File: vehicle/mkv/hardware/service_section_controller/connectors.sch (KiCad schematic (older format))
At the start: 5 parts, among them J401 MM_F_VT_16, J402 MM_F_VT_18, J403 MicroFit_VT_12, J404 Ultrafit_4_RA, J405 Ultrafit_4_RA

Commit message: incorporated feedback from dr
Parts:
- removed J402: MM_F_VT_18, footprints:micromatch_female_vert_18, symbol formula:MM_F_VT_18
- added J402: MM_F_VT_14, footprints:micromatch_female_vert_14, symbol formula:MM_F_VT_14
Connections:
- wire segments 13 -> 22
- no-connect marks 3 -> 0
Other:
- note added: "This needs to be a right angle connector"
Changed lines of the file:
@@
 Text GLabel 9050 1800 2    50   Input ~ 0
 FINAL_SHUTDOWN
-Text GLabel 6750 2750 2    50   Input ~ 0
+Text GLabel 6850 2050 2    50   Input ~ 0
 CHARGE_ENABLE1
-Text GLabel 6750 2850 2    50   Input ~ 0
+Text GLabel 6850 1850 2    50   Input ~ 0
 CHARGE_ENABLE2
-Text GLabel 6750 2950 2    50   Input ~ 0
+Text GLabel 6850 1950 2    50   Input ~ 0
 FAN_PWM
-Text GLabel 6750 2050 2    50   Input ~ 0
+Text GLabel 6850 2750 2    50   Input ~ 0
 CANL
-Text GLabel 6750 1950 2    50   Input ~ 0
-CANH
-Text GLabel 6750 2150 2    50   Input ~ 0
+Text GLabel 6850 2650 2    50   Input ~ 0
 TSAL_RED+
-Text GLabel 6750 2250 2    50   Input ~ 0
+Text GLabel 6850 2550 2    50   Input ~ 0
 TSAL_GREEN+
-Text GLabel 6750 2350 2    50   Input ~ 0
+Text GLabel 6850 2450 2    50   Input ~ 0
 TSAL_GREEN+
-Text GLabel 6750 2450 2    50   Input ~ 0
+Text GLabel 6850 2350 2    50   Input ~ 0
 TSAL_RED-
-Text GLabel 6750 2550 2    50   Input ~ 0
+Text GLabel 6850 2250 2    50   Input ~ 0
 TSAL_GREEN-
-Text GLabel 6750 2650 2    50   Input ~ 0
+Text GLabel 6850 2150 2    50   Input ~ 0
 TSAL_GREEN-
-Text GLabel 6750 3150 2    50   Input ~ 0
+Text GLabel 6850 1750 2    50   Input ~ 0
 BSPD_CURRENT_SENSE
-NoConn ~ 6750 3250
 Text GLabel 5100 3250 2    50   Input ~ 0
 SM_RJ45_LEDO
@@
 Text GLabel 5100 1950 2    50   Input ~ 0
 5V_BMS
-Wire Wire Line
-	6750 1850 7500 1850
-Wire Wire Line
-	7500 1850 7500 1700
-$Comp
-L power:+BATT #PWR?
-U 1 1 60F3FF06
-P 7500 1700
-F 0 "#PWR?" H 7500 1550 50  0001 C CNN
-F 1 "+BATT" H 7515 1873 50  0000 C CNN
-F 2 "" H 7500 1700 50  0001 C CNN
-F 3 "" H 7500 1700 50  0001 C CNN
-	1    7500 1700
-	1    0    0    -1
-$EndComp
-$Comp
-L power:GND #PWR?
-U 1 1 60FAB551
-P 7200 1550
-F 0 "#PWR?" H 7200 1300 50  0001 C CNN
-F 1 "GND" H 7205 1377 50  0000 C CNN
-F 2 "" H 7200 1550 50  0001 C CNN
-F 3 "" H 7200 1550 50  0001 C CNN
-	1    7200 1550
-	1    0    0    -1
-$EndComp
-Wire Wire Line
-	6750 1750 7000 1750
-Wire Wire Line
-	7000 1750 7000 1550
-Wire Wire Line
-	7000 1550 7200 1550
 $Comp
 L power:GND #PWR?
@@
 Wire Wire Line
 	6750 3050 8000 3050
+Wire Wire Line
+	6750 1850 6850 1850
+Wire Wire Line
+	6850 1750 6750 1750
+Wire Wire Line
+	6750 1950 6850 1950
 $Comp
-L formula:MM_F_VT_18 J402
-U 1 1 60C4104B
-P 6600 2850
-F 0 "J402" H 6558 4197 60  0000 C CNN
-F 1 "MM_F_VT_18" H 6558 4091 60  0000 C CNN
-F 2 "footprints:micromatch_female_vert_18" H 6400 3950 60  0001 C CNN
-F 3 "http://www.te.com/commerce/DocumentDelivery/DDEController?Action=showdoc&DocId=Customer+Drawing%7F338068%7FF1%7Fpdf%7FEnglish%7FENG_CD_338068_F1.pdf%7F1-338068-8" H 6500 4050 60  0001 C CNN
-F 4 "TE" H 6700 4250 60  0001 C CNN "MFN"
-F 5 "1-338068-8" H 6800 4350 60  0001 C CNN "MPN"
-F 6 "http://www.te.com/global-en/product-1-338068-8.html" H 6600 4150 60  0001 C CNN "PurchasingLink"
-	1    6600 2850
+L formula:MM_F_VT_14 J402
+U 1 1 61ED474B
+P 6450 2400
+F 0 "J402" H 6558 3297 60  0000 C CNN
+F 1 "MM_F_VT_14" H 6558 3191 60  0000 C CNN
+F 2 "footprints:micromatch_female_vert_14" H 6400 3050 60  0001 C CNN
+F 3 "http://www.te.com/commerce/DocumentDelivery/DDEController?Action=showdoc&DocId=Customer+Drawing%7F338068%7FF1%7Fpdf%7FEnglish%7FENG_CD_338068_F1.pdf%7F1-338068-4" H 6350 3600 60  0001 C CNN
+F 4 "TE" H 6550 3800 60  0001 C CNN "MFN"
+F 5 "1-338068-4" H 6650 3900 60  0001 C CNN "MPN"
+F 6 "http://www.te.com/global-en/product-1-338068-4.html" H 6450 3700 60  0001 C CNN "PurchasingLink"
+	1    6450 2400
 	1    0    0    -1
 $EndComp
-NoConn ~ 6750 3350
-NoConn ~ 6750 3450
+Text GLabel 6850 2850 2    50   Input ~ 0
+CANH
+$Comp
+L power:+BATT #PWR?
+U 1 1 61ED85B3
+P 7600 2900
+F 0 "#PWR?" H 7600 2750 50  0001 C CNN
+F 1 "+BATT" H 7615 3073 50  0000 C CNN
+F 2 "" H 7600 2900 50  0001 C CNN
+F 3 "" H 7600 2900 50  0001 C CNN
+	1    7600 2900
+	1    0    0    -1
+$EndComp
+Wire Wire Line
+	6750 2950 7600 2950
+Wire Wire Line
+	7600 2950 7600 2900
+Wire Wire Line
+	6750 2050 6850 2050
+Wire Wire Line
+	6750 2150 6850 2150
+Wire Wire Line
+	6750 2250 6850 2250
+Wire Wire Line
+	6750 2350 6850 2350
+Wire Wire Line
+	6750 2450 6850 2450
+Wire Wire Line
+	6750 2550 6850 2550
+Wire Wire Line
+	6750 2650 6850 2650
+Wire Wire Line
+	6750 2750 6850 2750
+Wire Wire Line
+	6750 2850 6850 2850
+Text Notes 6250 3250 0    50   ~ 0
+This needs to be a right angle connector
 $EndSCHEMATC

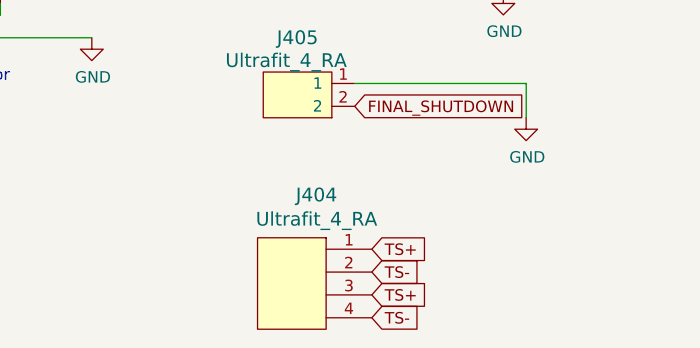
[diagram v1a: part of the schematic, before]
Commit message: complete service section controller layout, need to change some test point labels though
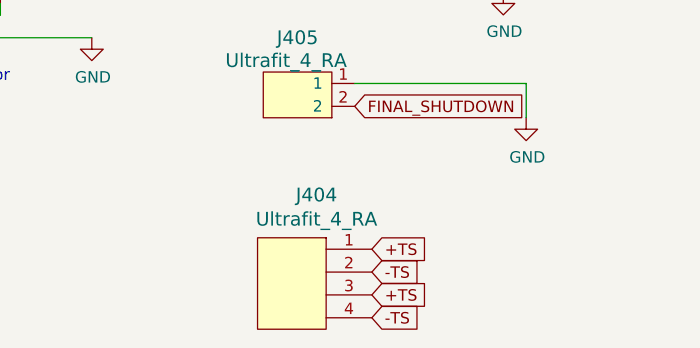
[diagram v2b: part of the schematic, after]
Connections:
- net TS+ renamed +TS
- net TS- renamed -TS
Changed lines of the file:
@@
 $EndComp
 Text GLabel 9225 3975 2    50   Input ~ 0
-TS+
++TS
 Text GLabel 9225 4075 2    50   Input ~ 0
-TS-
+-TS
 Text GLabel 9225 4175 2    50   Input ~ 0
-TS+
++TS
 Text GLabel 9225 4275 2    50   Input ~ 0
-TS-
+-TS
 Text Notes 1250 2600 0    50   ~ 0
 BMS isoSPI cutout on ‘BMS Core’ page for clarity

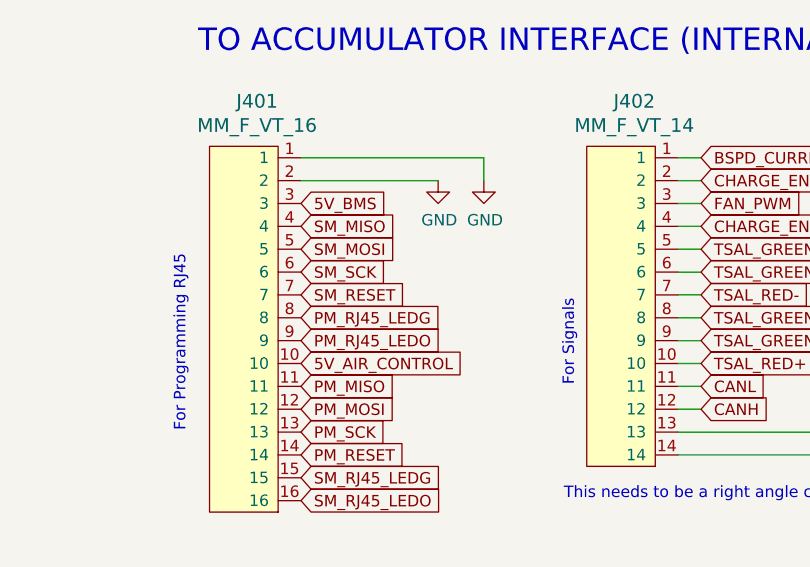
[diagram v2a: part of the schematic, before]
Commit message: commiting most recent changes, NOT finished layout yet
changed all 5V_BMS to +5V_BMS, 5V_AIR_CONTROL to +5V_AIR_CONTROL.
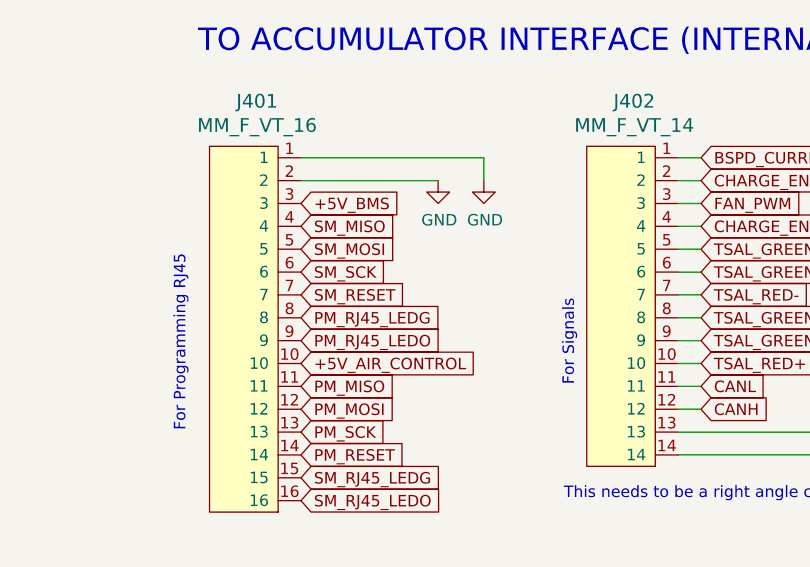
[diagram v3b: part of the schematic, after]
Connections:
- net 5V_AIR_CONTROL renamed +5V_AIR_CONTROL
- net 5V_BMS renamed +5V_BMS
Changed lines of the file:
@@
 PM_MISO
 Text GLabel 5100 2650 2    50   Input ~ 0
-5V_AIR_CONTROL
++5V_AIR_CONTROL
 Text GLabel 5100 2550 2    50   Input ~ 0
 PM_RJ45_LEDO
@@
 SM_MISO
 Text GLabel 5100 1950 2    50   Input ~ 0
-5V_BMS
++5V_BMS
 $Comp
 L power:GND #PWR?

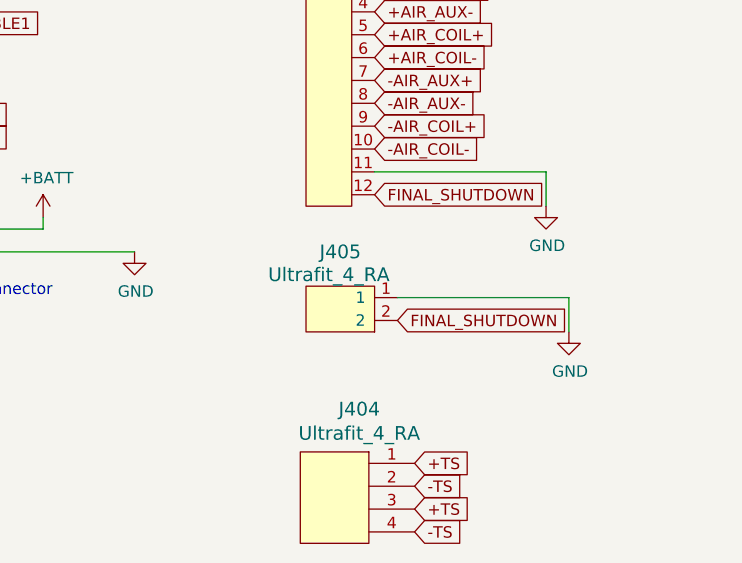
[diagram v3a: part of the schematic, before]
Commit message: Updated layout and added part to library
fixed shutdown current carrying traces - now 10mils
added the correct optoisolator footprint to library
added copper pour around tsal resistors for thermals

TODO:
move 400-15v regulator further down to make space for
a larger copper pour to improve thermals
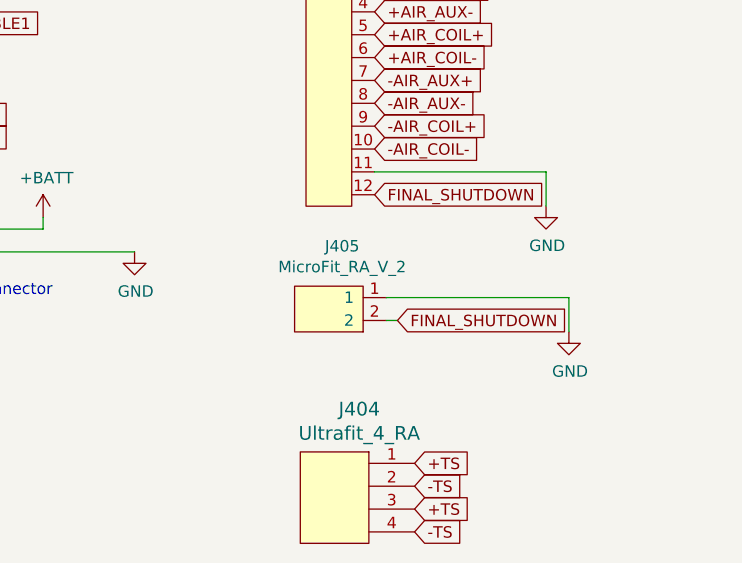
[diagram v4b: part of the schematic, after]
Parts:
- removed J405: Ultrafit_4_RA, footprints:Ultrafit_4_RA, symbol formula:MicroFit_V_2
- added J405: MicroFit_RA_V_2, footprints:MicroFit_RA_V_2, symbol formula:MicroFit_RA_V_2
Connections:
- net FINAL_SHUTDOWN: now also J405.2
- net GND: now also J405.1
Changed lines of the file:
@@
-	1    0    0    -1
-$EndComp
-$Comp
-L formula:MicroFit_V_2 J?
-U 1 1 60C16849
-P 8900 3300
-AR Path="/60A3B20D/60C16849" Ref="J?"  Part="1"
-AR Path="/60A3B236/60C16849" Ref="J?"  Part="1"
-AR Path="/60A3B41E/60C16849" Ref="J?"  Part="1"
-AR Path="/60A3B1F8/60C16849" Ref="J405"  Part="1"
-F 0 "J405" H 8900 3550 60  0000 C CNN
-F 1 "Ultrafit_4_RA" H 8850 3450 60  0000 C CNN
-F 2 "footprints:Ultrafit_4_RA" H 8400 3950 60  0001 C CNN
-F 3 "https://www.molex.com/pdm_docs/sd/1723101104_sd.pdf" H 9350 4400 60  0001 C CNN
-F 4 "Digi-Key" H 8200 4550 60  0001 C CNN "MFN"
-F 5 "Value" H 8050 3700 60  0001 C CNN "Package"
-F 6 "WM11574-ND" H 8250 3800 60  0001 C CNN "MPN"
-F 7 "WM11564-ND" H 9300 4050 60  0001 C CNN "MPN2"
-F 8 "https://www.digikey.com/products/en?keywords=1723101304" H 9400 4150 60  0001 C CNN "PurchasingLink"
-	1    8900 3300
 	1    0    0    -1
 $EndComp
@@
 Text GLabel 9150 3350 2    50   Input ~ 0
 FINAL_SHUTDOWN
-Wire Wire Line
-	9150 3250 9900 3250
 Wire Wire Line
 	9800 2700 9050 2700
@@
 Text Notes 6250 3250 0    50   ~ 0
 This needs to be a right angle connector
+$Comp
+L formula:MicroFit_RA_V_2 J405
+U 1 1 62060F67
+P 8850 3300
+F 0 "J405" H 8908 3575 50  0000 C CNN
+F 1 "MicroFit_RA_V_2" H 8908 3484 50  0000 C CNN
+F 2 "footprints:MicroFit_RA_V_2" H 8800 3500 50  0001 C CNN
+F 3 "https://www.molex.com/pdm_docs/sd/430450200_sd.pdf" H 8800 3500 50  0001 C CNN
+F 4 "MFN" H 8950 3550 50  0001 C CNN "DK"
+F 5 "WM1865-ND" H 9050 3650 50  0001 C CNN "MPN"
+F 6 "https://www.digikey.com/product-detail/en/molex/0430450200/WM1813-ND/252526" H 8850 3450 50  0001 C CNN "PurchasingLink"
+	1    8850 3300
+	1    0    0    -1
+$EndComp
+Wire Wire Line
+	9100 3250 9900 3250
+Wire Wire Line
+	9100 3350 9150 3350
 $EndSCHEMATC

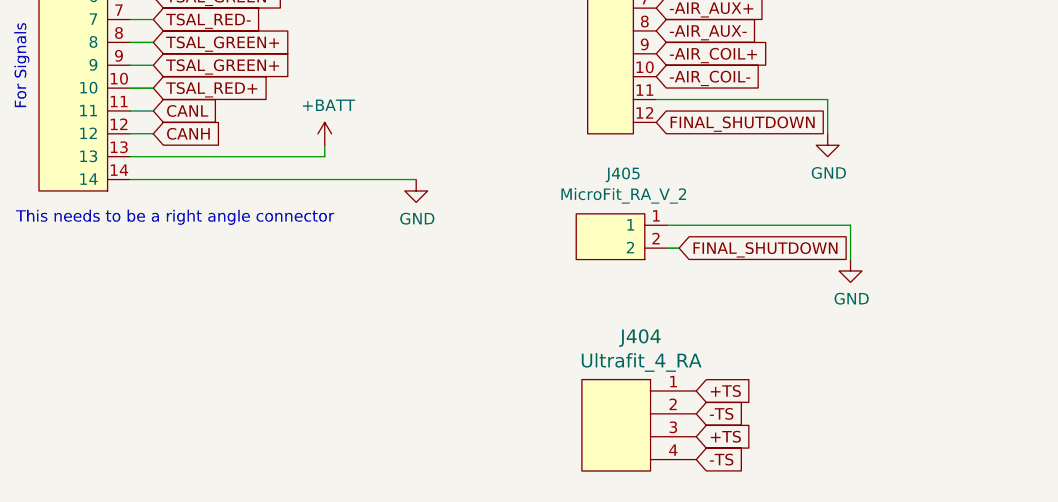
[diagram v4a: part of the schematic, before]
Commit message: Update service section controller for rev 2 (#139)
* Made changes for Rev 2 of SS controller schematic and layout

changed 12V IMD net to 5V IMD
to make layout changes easier, 5V IMD is supplied after 5V AIR control fuse
Power Main: Added larger test points for +Batt and GND for easier testing
IMD Latch: changed 12V nets to 5V, swapped inverting and non-inverting inputs for both op amps, removed resistor divider at IMD_STATUS_OUTPUT that goes to the ATmega
TSAL/AIL: changed 12V_TSAL to a 5V input, changed ts+ side resistor dividers to 1k and 120 (bottom of the op amp), changed AIL logic to use an nmos
Power Secondary: removed HV lin reg, added 15V - 5V lin reg and added a fuse for the 5V output. 400-15V lin reg can be used to provide 15V OR we can change resistors to provide 5V and short the output of lin reg to the output of the buck.
Micros: added a programming header for isospi for easier firmware testing, added test points for CANH and CANL for firmware debugging.

* Updated rev number on back silkscreen of PCB

* Make changes to Rev 2 of Service Section Controller Schematic and Layout

Updated IMD Latch resistor dividers.
Changed 5V lin reg capacitors to 2 1uF capacitors.
Added a protection diode for lin reg.
Added a 0 Ohm jumper between 5V tsal and 15V buck output in case the buck converter can output 5V and we no longer need the lin reg.
Spread out the tsal resistors to help with heat dissipation.

* Added a few silkscreen labels for 0Ohm jumpers.

* Shifted connectors and edited track lengths

Changed IMD connector to a 6-pin microfit.
Rotated BMS connector to face upwards to avoid clearance issues.
added silkscreen for more clarity.

* Added final revisions for 2nd version of service section controller

Changed IMD connector to a RA footprint (same footprint as VT tho)
Changed Shutdown connector to an 8-pin RA microfit
Changed TS connector to a 4 pin VT microfit
shifted BMS connector slighly
changed bms and air control prog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
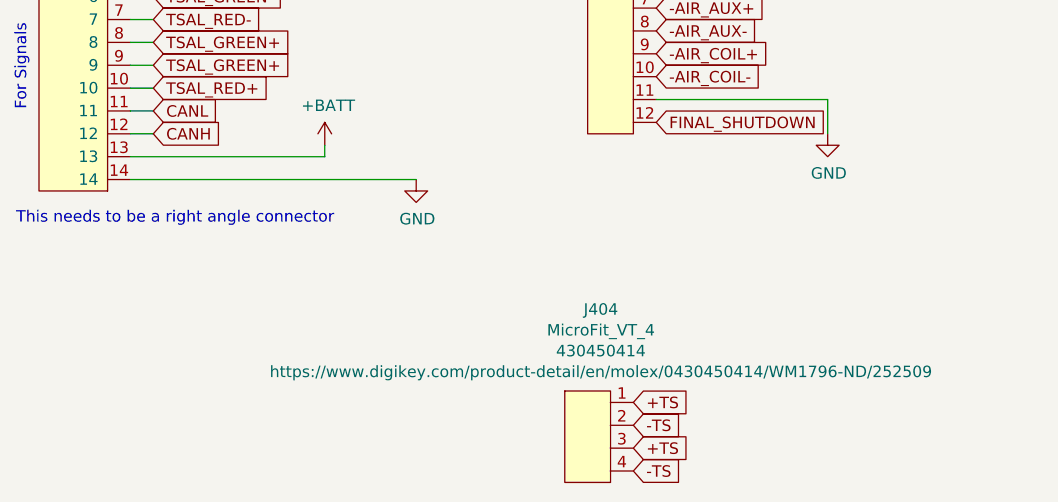
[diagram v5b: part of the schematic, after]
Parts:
- removed J404: Ultrafit_4_RA, footprints:Ultrafit_4_RA, symbol formula:Ultrafit_4_RA
- removed J405: MicroFit_RA_V_2, footprints:MicroFit_RA_V_2, symbol formula:MicroFit_RA_V_2
- added J404: MicroFit_VT_4, footprints:MicroFit_VT_4, symbol formula:MicroFit_VT_4
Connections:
- net +TS: now also J404.1, J404.3
- net -TS: now also J404.2, J404.4
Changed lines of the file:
@@
 For Signals
-$Comp
-L power:GND #PWR?
-U 1 1 60E61A8C
-P 9900 3400
-AR Path="/60A3B20D/60E61A8C" Ref="#PWR?"  Part="1"
-AR Path="/60A3B1F8/60E61A8C" Ref="#PWR?"  Part="1"
-F 0 "#PWR?" H 9900 3150 50  0001 C CNN
-F 1 "GND" H 9905 3227 50  0000 C CNN
-F 2 "" H 9900 3400 50  0001 C CNN
-F 3 "" H 9900 3400 50  0001 C CNN
-	1    9900 3400
-	1    0    0    -1
-$EndComp
-Wire Wire Line
-	9900 3400 9900 3250
 $Comp
 L formula:MicroFit_VT_12 J?
@@
 	1    0    0    -1
 $EndComp
-$Comp
-L formula:Ultrafit_4_RA J?
-U 1 1 60B785AF
-P 8875 4175
-AR Path="/60A3B236/60B785AF" Ref="J?"  Part="1"
-AR Path="/60A3B41E/60B785AF" Ref="J?"  Part="1"
-AR Path="/60A3B1F8/60B785AF" Ref="J404"  Part="1"
-F 0 "J404" H 8983 4612 60  0000 C CNN
-F 1 "Ultrafit_4_RA" H 8983 4506 60  0000 C CNN
-F 2 "footprints:Ultrafit_4_RA" H 8375 4825 60  0001 C CNN
-F 3 "https://www.molex.com/pdm_docs/sd/1723101104_sd.pdf" H 9325 5275 60  0001 C CNN
-F 4 "Digi-Key" H 8175 5425 60  0001 C CNN "MFN"
-F 5 "Value" H 8025 4575 60  0001 C CNN "Package"
-F 6 "WM11574-ND" H 8225 4675 60  0001 C CNN "MPN"
-F 7 "WM11564-ND" H 9275 4925 60  0001 C CNN "MPN2"
-F 8 "https://www.digikey.com/products/en?keywords=1723101304" H 9375 5025 60  0001 C CNN "PurchasingLink"
-	1    8875 4175
-	1    0    0    -1
-$EndComp
-Text GLabel 9225 3975 2    50   Input ~ 0
+Text GLabel 8950 4025 2    50   Input ~ 0
 +TS
-Text GLabel 9225 4075 2    50   Input ~ 0
+Text GLabel 8950 4125 2    50   Input ~ 0
 -TS
-Text GLabel 9225 4175 2    50   Input ~ 0
+Text GLabel 8950 4225 2    50   Input ~ 0
 +TS
-Text GLabel 9225 4275 2    50   Input ~ 0
+Text GLabel 8950 4325 2    50   Input ~ 0
 -TS
 Text Notes 1250 2600 0    50   ~ 0
@@
 +AIR_AUX+
 Text GLabel 9050 2800 2    50   Input ~ 0
-FINAL_SHUTDOWN
-Text GLabel 9150 3350 2    50   Input ~ 0
 FINAL_SHUTDOWN
 Wire Wire Line
@@
 This needs to be a right angle connector
 $Comp
-L formula:MicroFit_RA_V_2 J405
-U 1 1 62060F67
-P 8850 3300
-F 0 "J405" H 8908 3575 50  0000 C CNN
-F 1 "MicroFit_RA_V_2" H 8908 3484 50  0000 C CNN
-F 2 "footprints:MicroFit_RA_V_2" H 8800 3500 50  0001 C CNN
-F 3 "https://www.molex.com/pdm_docs/sd/430450200_sd.pdf" H 8800 3500 50  0001 C CNN
-F 4 "MFN" H 8950 3550 50  0001 C CNN "DK"
-F 5 "WM1865-ND" H 9050 3650 50  0001 C CNN "MPN"
-F 6 "https://www.digikey.com/product-detail/en/molex/0430450200/WM1813-ND/252526" H 8850 3450 50  0001 C CNN "PurchasingLink"
-	1    8850 3300
-	1    0    0    -1
-$EndComp
-Wire Wire Line
-	9100 3250 9900 3250
-Wire Wire Line
-	9100 3350 9150 3350
+L formula:MicroFit_VT_4 J404
+U 1 1 6267E8D8
+P 8750 4175
+F 0 "J404" H 8808 4732 50  0000 C CNN
+F 1 "MicroFit_VT_4" H 8808 4641 50  0000 C CNN
+F 2 "footprints:MicroFit_VT_4" H 8750 3875 50  0001 C CNN
+F 3 "" H 8750 4125 50  0001 C CNN
+F 4 "430450414" H 8808 4550 50  0000 C CNN "MPN"
+F 5 "https://www.digikey.com/product-detail/en/molex/0430450414/WM1796-ND/252509" H 8808 4459 50  0000 C CNN "PurchasingLink"
+	1    8750 4175
+	1    0    0    -1
+$EndComp
 $EndSCHEMATC
